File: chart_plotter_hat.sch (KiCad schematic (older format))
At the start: 34 parts, among them J1 Conn_02x03_Odd_Even, J10 Conn_01x04, J11 Conn_02x03_Odd_Even, J2 Conn_01x04, J3 40HAT, J5 Conn_02x04_Odd_Even, J6 Conn_01x02, Q1 DMG2305UX, Q2 DMMT5401, U1 ATmega328P-AU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

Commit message: many changes
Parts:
- added C6, C7: .1uF, Capacitors_SMD:C_0603_HandSoldering, symbol Device:C
- C1, C5: value .01uF -> .1uF
- C2: footprint Capacitors_SMD:C_0603_HandSoldering -> Capacitors_SMD:C_1206
- R2: value 412 -> 680
- R3: value 1K -> 330
- R4: value 1K -> 680
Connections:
- net labels removed: EN_VIDEO
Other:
- note added: "3.3V Power"
- note added: "5V Power"
- note added: "EEPROM Bypass Cap"
- note added: "Power Monitor MCU"
- note added: "Video Power"
- note removed: "This is the recommended 5V rail protection for \na HAT with power going to the Pi.\nSee https://github.com/raspberrypi/hats/blob/master/designguide.md#back-powering-the-pi-via-the-j8-gpio-header"
- note removed: "Video Power Connector"
- moved on the sheet: D2, J1, J10, J5, R3

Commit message: Changed SS relay to a G3VM-201FR
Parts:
- removed U5: ASSR-1218, Housings_SOIC:SO-4_4.4x4.3mm_Pitch2.54mm, symbol Relay_SolidState:ASSR-1218
- added U5: G3VM-201FR, Housings_DIP:DIP-8_W8.89mm_SMDSocket_LongPads, symbol CustomComponents:G3VM-201FR
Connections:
- wire segments 140 -> 137
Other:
- moved on the sheet: J6, R2
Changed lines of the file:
@@
 L Connector_Generic:Conn_01x02 J6
 U 1 1 5FEFCBF8
-P 4825 9525
-F 0 "J6" H 4905 9517 50  0000 L CNN
-F 1 "Conn_01x02" H 4905 9426 50  0000 L CNN
-F 2 "Pin_Headers:Pin_Header_Straight_1x02_Pitch2.00mm" H 4825 9525 50  0001 C CNN
-F 3 "~" H 4825 9525 50  0001 C CNN
-	1    4825 9525
-	1    0    0    -1
-$EndComp
-Text Notes 4175 8350 0    118  ~ 24
+P 4825 9500
+F 0 "J6" H 4905 9492 50  0000 L CNN
+F 1 "Conn_01x02" H 4905 9401 50  0000 L CNN
+F 2 "Pin_Headers:Pin_Header_Straight_1x02_Pitch2.00mm" H 4825 9500 50  0001 C CNN
+F 3 "~" H 4825 9500 50  0001 C CNN
+	1    4825 9500
+	1    0    0    -1
+$EndComp
+Text Notes 3650 9150 0    118  ~ 24
 Video Power
-$Comp
-L power:GND #PWR0111
-U 1 1 5FF08C70
-P 4625 9625
-F 0 "#PWR0111" H 4625 9375 50  0001 C CNN
-F 1 "GND" H 4625 9475 50  0000 C CNN
-F 2 "" H 4625 9625 50  0000 C CNN
-F 3 "" H 4625 9625 50  0000 C CNN
-	1    4625 9625
-	1    0    0    -1
-$EndComp
-$Comp
-L Relay_SolidState:ASSR-1218 U5
-U 1 1 5FF0E3EE
-P 4125 8900
-F 0 "U5" H 4125 9225 50  0000 C CNN
-F 1 "ASSR-1218" H 4125 9134 50  0000 C CNN
-F 2 "Housings_SOIC:SO-4_4.4x4.3mm_Pitch2.54mm" H 3925 8700 50  0001 L CIN
-F 3 "https://docs.broadcom.com/docs/AV02-0173EN" H 4125 8900 50  0001 L CNN
-	1    4125 8900
-	1    0    0    -1
-$EndComp
 $Comp
 L power:+12V #PWR0112
 U 1 1 5FF1CC91
-P 4575 8700
-F 0 "#PWR0112" H 4575 8550 50  0001 C CNN
-F 1 "+12V" H 4590 8873 50  0000 C CNN
-F 2 "" H 4575 8700 50  0001 C CNN
-F 3 "" H 4575 8700 50  0001 C CNN
-	1    4575 8700
-	1    0    0    -1
-$EndComp
-Wire Wire Line
-	4425 8800 4575 8800
-Wire Wire Line
-	4575 8800 4575 8700
+P 4625 9500
+F 0 "#PWR0112" H 4625 9350 50  0001 C CNN
+F 1 "+12V" H 4640 9673 50  0000 C CNN
+F 2 "" H 4625 9500 50  0001 C CNN
+F 3 "" H 4625 9500 50  0001 C CNN
+	1    4625 9500
+	1    0    0    -1
+$EndComp
 $Comp
 L power:GND #PWR0113
 U 1 1 5FF37278
-P 3675 9100
-F 0 "#PWR0113" H 3675 8850 50  0001 C CNN
-F 1 "GND" H 3675 8950 50  0000 C CNN
-F 2 "" H 3675 9100 50  0000 C CNN
-F 3 "" H 3675 9100 50  0000 C CNN
-	1    3675 9100
-	1    0    0    -1
-$EndComp
-Wire Wire Line
-	3825 9000 3675 9000
-Wire Wire Line
-	3675 9000 3675 9100
-Wire Wire Line
-	3700 8800 3825 8800
+P 3625 9775
+F 0 "#PWR0113" H 3625 9525 50  0001 C CNN
+F 1 "GND" H 3625 9625 50  0000 C CNN
+F 2 "" H 3625 9775 50  0000 C CNN
+F 3 "" H 3625 9775 50  0000 C CNN
+	1    3625 9775
+	1    0    0    -1
+$EndComp
 $Comp
 L Device:R R2
 U 1 1 5FF8607A
-P 3550 8800
-F 0 "R2" V 3630 8800 50  0000 C CNN
-F 1 "680" V 3550 8800 50  0000 C CNN
-F 2 "Resistors_SMD:R_0603_HandSoldering" V 3480 8800 50  0001 C CNN
-F 3 "" H 3550 8800 50  0001 C CNN
-	1    3550 8800
+P 3350 9550
+F 0 "R2" V 3430 9550 50  0000 C CNN
+F 1 "680" V 3350 9550 50  0000 C CNN
+F 2 "Resistors_SMD:R_0603_HandSoldering" V 3280 9550 50  0001 C CNN
+F 3 "" H 3350 9550 50  0001 C CNN
+	1    3350 9550
 	0    1    1    0
 $EndComp
@@
 	1    0    0    -1
 $EndComp
-Wire Wire Line
-	4425 9000 4500 9000
-Wire Wire Line
-	4500 9000 4500 9525
-Wire Wire Line
-	4500 9525 4625 9525
 Text GLabel 14300 5025 0    50   Input ~ 0
 A6
@@
 $EndComp
 Wire Wire Line
-	3400 8800 3150 8800
-Text Label 3200 8800 0    50   ~ 0
+	3200 9550 2950 9550
+Text Label 3000 9550 0    50   ~ 0
 P5V
 $Comp
@@
 Wire Wire Line
 	13125 6500 13125 6650
+$Comp
+L CustomComponents:G3VM-201FR U5
+U 1 1 5FEC1F34
+P 3925 9600
+F 0 "U5" H 3925 9925 50  0000 C CNN
+F 1 "G3VM-201FR" H 3925 9834 50  0000 C CNN
+F 2 "Housings_DIP:DIP-8_W8.89mm_SMDSocket_LongPads" H 3946 9164 50  0001 C CNN
+F 3 "https://toshiba.semicon-storage.com/info/docget.jsp?did=12660&prodName=TLP3543" H 3925 9450 50  0001 C CNN
+	1    3925 9600
+	1    0    0    -1
+$EndComp
+Wire Wire Line
+	3500 9550 3625 9550
+Wire Wire Line
+	4625 9500 4225 9500
+Wire Wire Line
+	4625 9600 4350 9600
+Wire Wire Line
+	4350 9600 4350 9850
+Wire Wire Line
+	4350 9850 4225 9850
+Connection ~ 4350 9850
+Connection ~ 4625 9500
+$Comp
+L power:GND #PWR?
+U 1 1 5FF51245
+P 4350 9850
+F 0 "#PWR?" H 4350 9600 50  0001 C CNN
+F 1 "GND" H 4350 9700 50  0000 C CNN
+F 2 "" H 4350 9850 50  0000 C CNN
+F 3 "" H 4350 9850 50  0000 C CNN
+	1    4350 9850
+	1    0    0    -1
+$EndComp
 $EndSCHEMATC

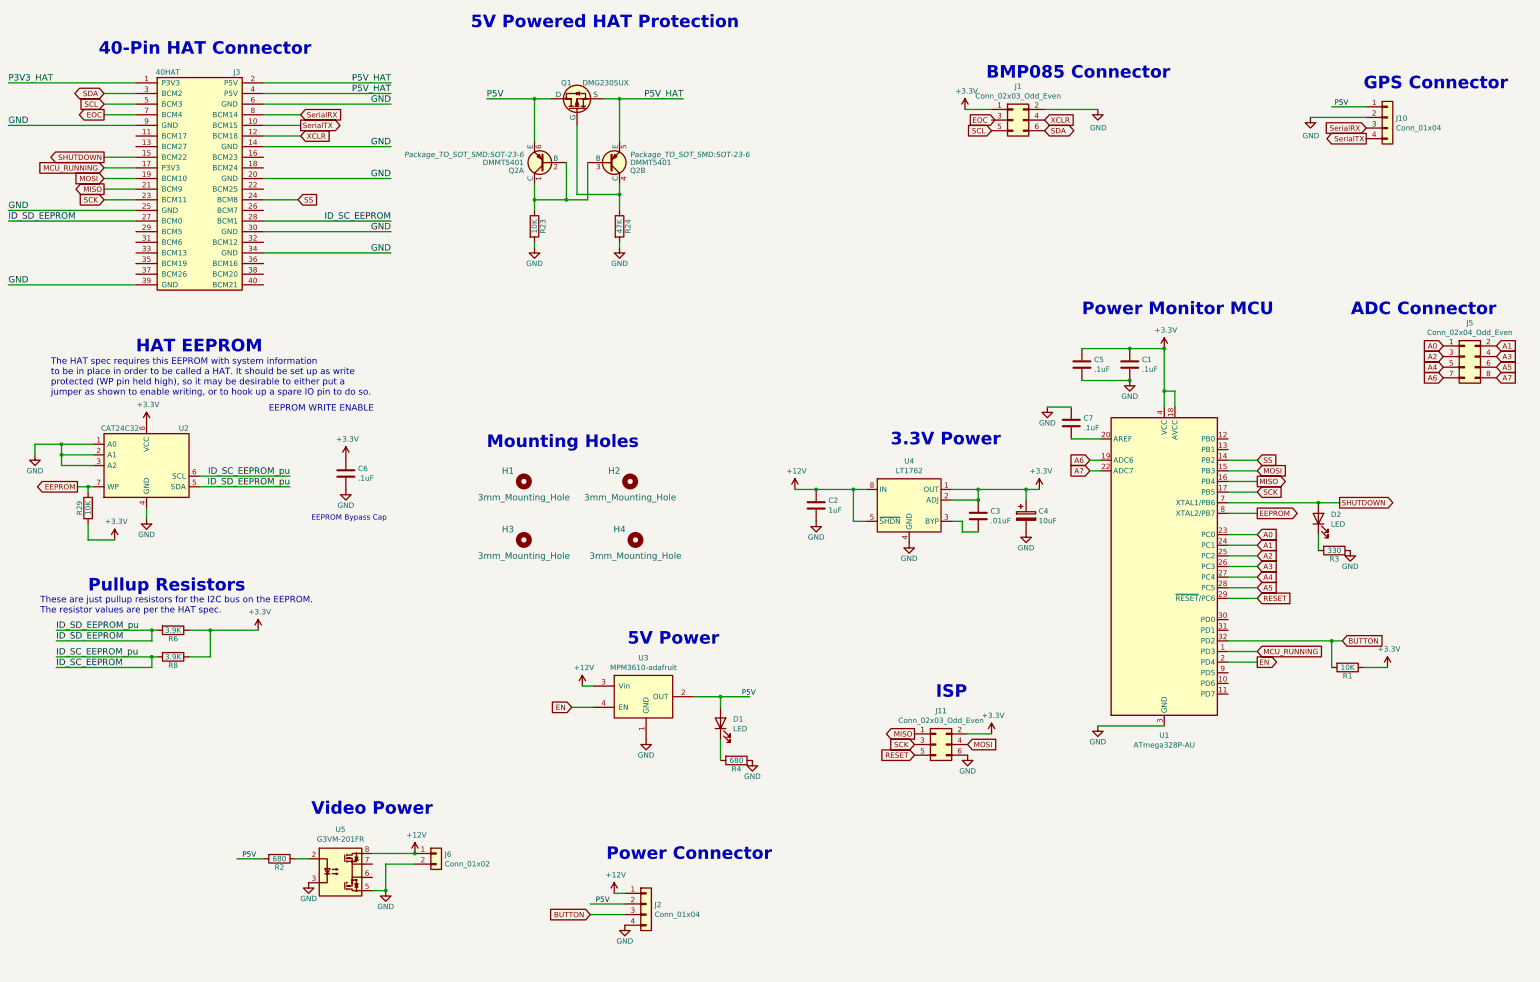
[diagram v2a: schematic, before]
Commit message: Changed footprints to non-solder
changed headers to JST-PH connectors
changed mask clearance
Connected EOC
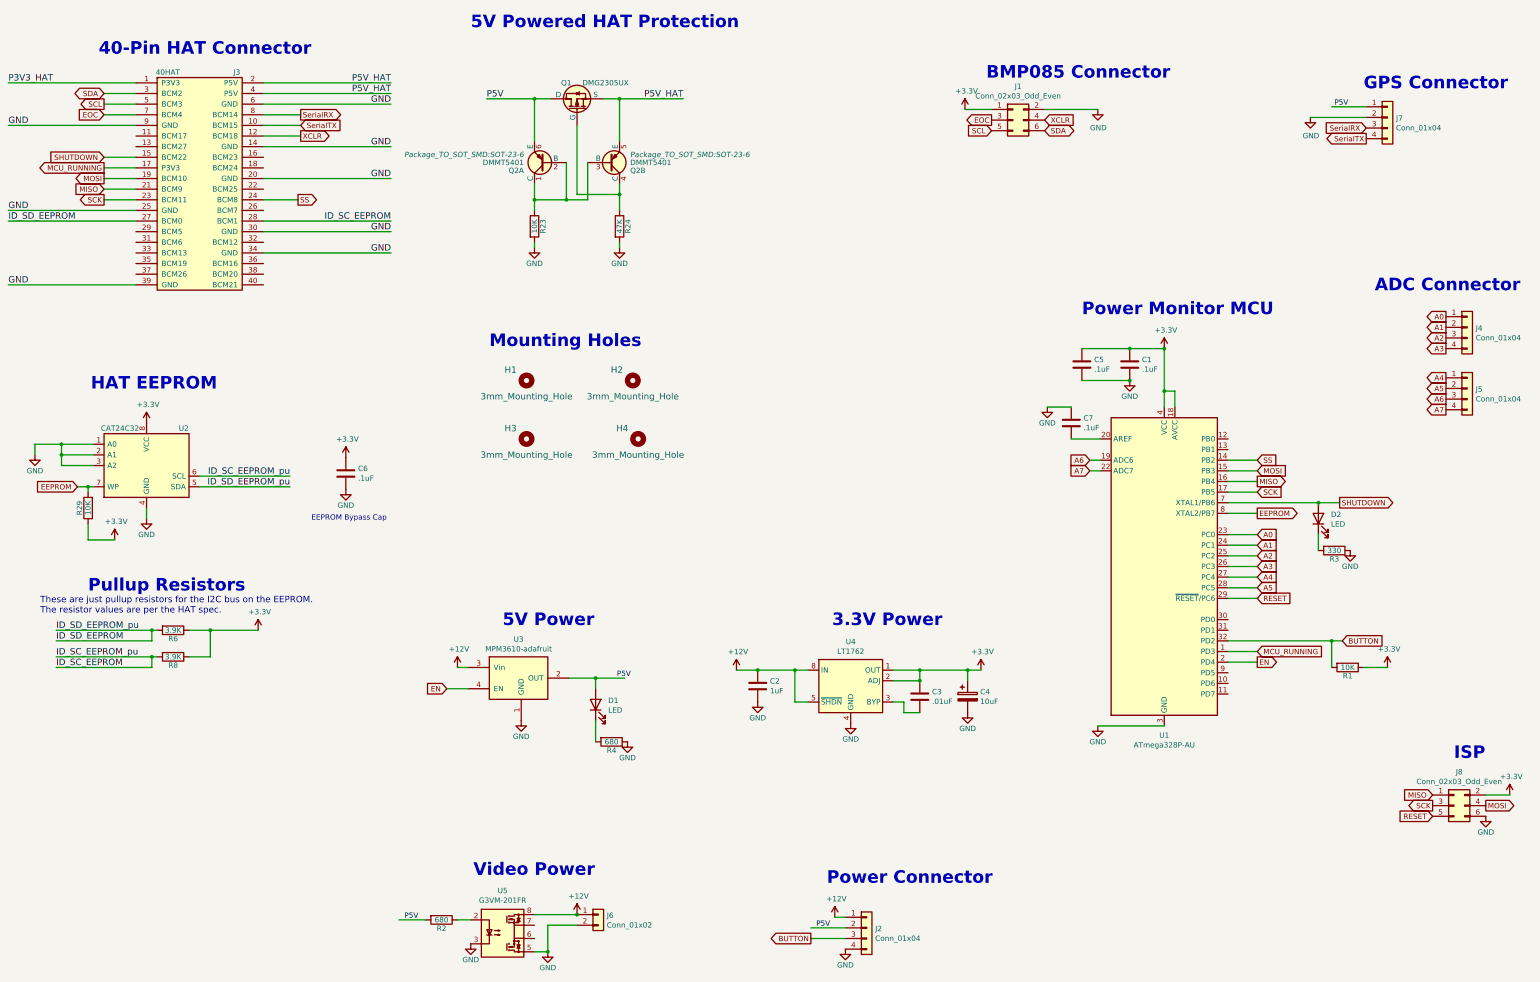
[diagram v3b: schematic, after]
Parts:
- removed J5: Conn_02x04_Odd_Even, Pin_Headers:Pin_Header_Straight_2x04_Pitch2.00mm, symbol Connector_Generic:Conn_02x04_Odd_Even
- added J4, J5: Conn_01x04, Connectors_JST:JST_PH_B4B-PH-K_04x2.00mm_Straight, symbol Connector_Generic:Conn_01x04
- C1, C3, C5, C6, C7: footprint Capacitors_SMD:C_0603_HandSoldering -> Capacitors_SMD:C_0603
- D1, D2: footprint LEDs:LED_0603_HandSoldering -> LEDs:LED_0603
- J1: footprint Pin_Headers:Pin_Header_Straight_2x03_Pitch2.54mm -> CustomComponents:BOX-HEADER6
- J2: footprint Pin_Headers:Pin_Header_Straight_1x04_Pitch2.00mm -> Connectors_JST:JST_PH_B4B-PH-K_04x2.00mm_Straight
- J6: footprint Pin_Headers:Pin_Header_Straight_1x02_Pitch2.00mm -> Connectors_JST:JST_PH_B2B-PH-K_02x2.00mm_Straight
- J7: renamed from J10; footprint Pin_Headers:Pin_Header_Straight_1x04_Pitch2.00mm -> Connectors_JST:JST_PH_B4B-PH-K_04x2.00mm_Straight
- R1, R2, R3, R4: footprint Resistors_SMD:R_0603_HandSoldering -> Resistors_SMD:R_0603
- R23, R24, R29, R6, R8: footprint Resistor_SMD:R_0603_1608Metric_Pad0.84x1.00mm_HandSolder -> Resistors_SMD:R_0603
- renumbered J11 to J8
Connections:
- net A0: now also J4.1 (Pin_1)
- net A1: now also J4.2 (Pin_2)
- net A2: now also J4.3 (Pin_3)
- net A3: now also J4.4 (Pin_4)
- net A4: now also J5.1 (Pin_1)
- net A5: now also J5.2 (Pin_2)
- net A6: now also J5.3 (Pin_3)
- net A7: now also J5.4 (Pin_4)
- net EOC: now also J1.3 (Pin_3)
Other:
- note removed: "EEPROM WRITE ENABLE"
- note removed: "The HAT spec requires this EEPROM with system information\nto be in place in order to be called a HAT. It should be set up as write\nprotected (WP pin held high), so it may be desirable to either put a \njumper as shown to enable writing, or to hook up a spare IO pin to do so."
- moved on the sheet: C2, C3, C4, D1, H1, H2, H3, H4, J2, J6, J8, R2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

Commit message: MCU_RUNNING was connected to P3.3V on header
Moved MCU_RUNNING to a gpio pin
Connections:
- net MCU_RUNNING: now also J3.16 (BCM23); no longer J3.17 (P3V3)
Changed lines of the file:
@@
 Title "Chart Plotter Hat"
 Date ""
-Rev "A"
+Rev "B"
 Comp "bit-builder.com"
 Comment1 ""
@@
 Text GLabel 1700 2950 0    50   Input ~ 0
 SHUTDOWN
-Text GLabel 1700 3050 0    50   Output ~ 0
+Text GLabel 3550 2950 2    50   Output ~ 0
 MCU_RUNNING
 $Comp
@@
 $EndComp
 Wire Wire Line
-	2000 3050 1700 3050
-Wire Wire Line
 	2000 2950 1700 2950
 $Comp
@@
 	1    0    0    -1
 $EndComp
+Wire Wire Line
+	3200 2950 3550 2950
 $EndSCHEMATC

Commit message: Added pulldown R10 on MCU_RUNNING
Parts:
- added R10: 10K, Resistors_SMD:R_0603, symbol Device:R
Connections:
- net GND: now also R10.1
- net MCU_RUNNING: now also R10.2
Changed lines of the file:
@@
 Text GLabel 13325 6200 2    50   Output ~ 0
 SHUTDOWN
-Text GLabel 12550 7600 2    50   Input ~ 0
+Text GLabel 13225 8025 2    50   Input ~ 0
 MCU_RUNNING
 Text GLabel 13350 7500 2    50   Input ~ 0
@@
 	12275 7500 13250 7500
 Wire Wire Line
-	12275 7600 12550 7600
-Wire Wire Line
 	12275 6200 13125 6200
 $Comp
 L power:GND #PWR015
 U 1 1 5FDCD1F3
-P 11050 8300
-F 0 "#PWR015" H 11050 8050 50  0001 C CNN
-F 1 "GND" H 11050 8150 50  0000 C CNN
-F 2 "" H 11050 8300 50  0000 C CNN
-F 3 "" H 11050 8300 50  0000 C CNN
-	1    11050 8300
+P 13050 8325
+F 0 "#PWR015" H 13050 8075 50  0001 C CNN
+F 1 "GND" H 13050 8175 50  0000 C CNN
+F 2 "" H 13050 8325 50  0000 C CNN
+F 3 "" H 13050 8325 50  0000 C CNN
+	1    13050 8325
 	1    0    0    -1
 $EndComp
@@
 Wire Wire Line
 	3200 2950 3550 2950
+Wire Wire Line
+	13050 7600 13050 8025
+Wire Wire Line
+	13050 8025 13225 8025
+Wire Wire Line
+	12275 7600 13050 7600
+$Comp
+L Device:R R10
+U 1 1 5FF805D9
+P 13050 8175
+F 0 "R10" V 13130 8175 50  0000 C CNN
+F 1 "10K" V 13050 8175 50  0000 C CNN
+F 2 "Resistors_SMD:R_0603" V 12980 8175 50  0001 C CNN
+F 3 "" H 13050 8175 50  0001 C CNN
+	1    13050 8175
+	-1   0    0    1
+$EndComp
+Connection ~ 13050 8025
+$Comp
+L power:GND #PWR?
+U 1 1 5FFA1E86
+P 11050 8300
+F 0 "#PWR?" H 11050 8050 50  0001 C CNN
+F 1 "GND" H 11050 8150 50  0000 C CNN
+F 2 "" H 11050 8300 50  0000 C CNN
+F 3 "" H 11050 8300 50  0000 C CNN
+	1    11050 8300
+	1    0    0    -1
+$EndComp
 $EndSCHEMATC
